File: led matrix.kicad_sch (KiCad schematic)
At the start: 88 parts, among them SW49 Slide_DPDT_SS22D06

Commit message: parpar v2 RC2
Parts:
- added JP3: Switch bypass, Jumper:SolderJumper-2_P1.3mm_Open_TrianglePad1.0x1.5mm, symbol Jumper:SolderJumper_2_Open
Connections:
- net +5V: now also JP3.1 (A)
- net PRI_LO: now also JP3.2 (B)
- net led_data: now also R1.2; no longer R1.1
- net at D3.3 (DIN): now also R1.1; no longer R1.2
- net led_out: now reaches D44.2 (DOUT)
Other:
- moved on the sheet: JP1

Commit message: parpar v2 RC3
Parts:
- R1: symbol Device:R -> Device:R_US
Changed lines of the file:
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@@
 	)
 	(symbol
-		(lib_id "Device:R")
+		(lib_id "Device:R_US")
 		(at 16.51 33.02 0)
 		(mirror x)
@@
 		(on_board yes)
 		(dnp no)
-		(fields_autoplaced yes)
 		(property "Reference" "R1"
-			(at 19.05 34.2901 0)
+			(at 19.304 33.782 90)
 			(effects
 				(font
 					(size 1.27 1.27)
 				)
-				(justify left)
+				(justify right)
 			)
 		)
 		(property "Value" "R470"
-			(at 19.05 31.7501 0)
+			(at 21.59 34.798 90)
 			(effects
 				(font
 					(size 1.27 1.27)
 				)
-				(justify left)
+				(justify right)
 			)
 		)
 		(property "Footprint" "Resistor_SMD:R_0805_2012Metric"
-			(at 14.732 33.02 90)
+			(at 17.526 32.766 90)
 			(effects
 				(font
@@
 			)
 		)
-		(property "Description" "Resistor"
+		(property "Description" "Resistor, US symbol"
 			(at 16.51 33.02 0)
 			(effects

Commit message: parpar v2 RC4
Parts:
- removed JP3: Switch bypass, Jumper:SolderJumper-2_P1.3mm_Open_TrianglePad1.0x1.5mm, symbol Jumper:SolderJumper_2_Open
- removed SW49: Slide_DPDT_SS22D06, Button_Switch_SMD:SW_DPDT_CK_JS202011JCQN, symbol PCM_4ms_Switch:Slide_DPDT_SS22D06
- added C48: 0.1uF, Capacitor_SMD:C_0805_2012Metric, symbol Device:C
- added R6: R500, Resistor_SMD:R_0805_2012Metric, symbol Device:R_US
- added R7: 10k, Resistor_SMD:R_0805_2012Metric, symbol Device:R_US
- added U13: SN74LV1T125DCK, Package_TO_SOT_SMD:SOT-353_SC-70-5, symbol Logic_LevelTranslator:SN74LV1T125DCK
- R1: value R470 -> R500
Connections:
- net PRI_LO is gone; now on net +5V: C1.1, C10.1, C11.1, C12.1, C13.1, C14.1, C15.1, C16.1, C17.1, C18.1, C19.1, C2.1, C20.1, C21.1, C22.1, C23.1, C24.1, C25.1, C26.1, C27.1, C28.1, C29.1, C3.1, C30.1, C31.1, C32.1, C33.1, C34.1, C35.1, C36.1, C37.1, C38.1, C39.1, C4.1, C40.1, C41.1, C42.1, C43.1, C5.1, C6.1, C7.1, C8.1, C9.1, D10.1 (VDD), D11.1 (VDD), D12.1 (VDD), D13.1 (VDD), D14.1 (VDD), D15.1 (VDD), D16.1 (VDD), D17.1 (VDD), D18.1 (VDD), D19.1 (VDD), D20.1 (VDD), D21.1 (VDD), D22.1 (VDD), D23.1 (VDD), D24.1 (VDD), D25.1 (VDD), D26.1 (VDD), D27.1 (VDD), D28.1 (VDD), D29.1 (VDD), D3.1 (VDD), D30.1 (VDD), D31.1 (VDD), D32.1 (VDD), D33.1 (VDD), D34.1 (VDD), D35.1 (VDD), D36.1 (VDD), D37.1 (VDD), D38.1 (VDD), D39.1 (VDD), D4.1 (VDD), D40.1 (VDD), D41.1 (VDD), D42.1 (VDD), D43.1 (VDD), D44.1 (VDD), D5.1 (VDD), D6.1 (VDD), D7.1 (VDD), D8.1 (VDD), D9.1 (VDD)
- net +5V: now also C48.1
- net GND: now also R7.1, U13.3 (GND)
- net led_data: now also U13.4 (Y); no longer JP1.2 (C)
- net led_out: now also R6.2; no longer D44.2 (DOUT)
- new net: R7.2, U13.1 (~{OE})
- new net: C48.2, U13.5 (VCC)
- new net: D44.2 (DOUT), R6.1
- new net led_data_in: JP1.2 (C), U13.2 (A)
- no-connect marks 1 -> 0
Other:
- note added: "led data"
- note added: "led power input"
- note removed: "led data selector"
- note removed: "led power switch"
- moved on the sheet: C1, C10, C11, C12, C13, C14, C15, C16, C17, C18, C19, C2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

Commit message: parpar v2 RC6
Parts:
- JP1: value SolderJumper_3_Bridged12 -> data select
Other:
- note added: "rgb data"
- note added: "rgb power in"
- note removed: "led data"
- note removed: "led power input"
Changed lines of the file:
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@@
 	)
 	(rectangle
-		(start 172.72 78.74)
+		(start 173.355 72.39)
 		(end 284.48 160.02)
 		(stroke
@@
 		)
 	)
-	(text "led data"
+	(text "rgb data"
 		(exclude_from_sim no)
-		(at 218.948 16.51 0)
+		(at 214.884 16.764 0)
 		(effects
 			(font
@@
 		)
 	)
-	(text "led power input"
+	(text "rgb power in"
 		(exclude_from_sim no)
-		(at 181.61 16.51 0)
+		(at 179.832 16.764 0)
 		(effects
 			(font
@@
 			)
 		)
-		(property "Value" "SolderJumper_3_Bridged12"
+		(property "Value" "data select"
 			(at 228.6 24.13 0)
 			(effects

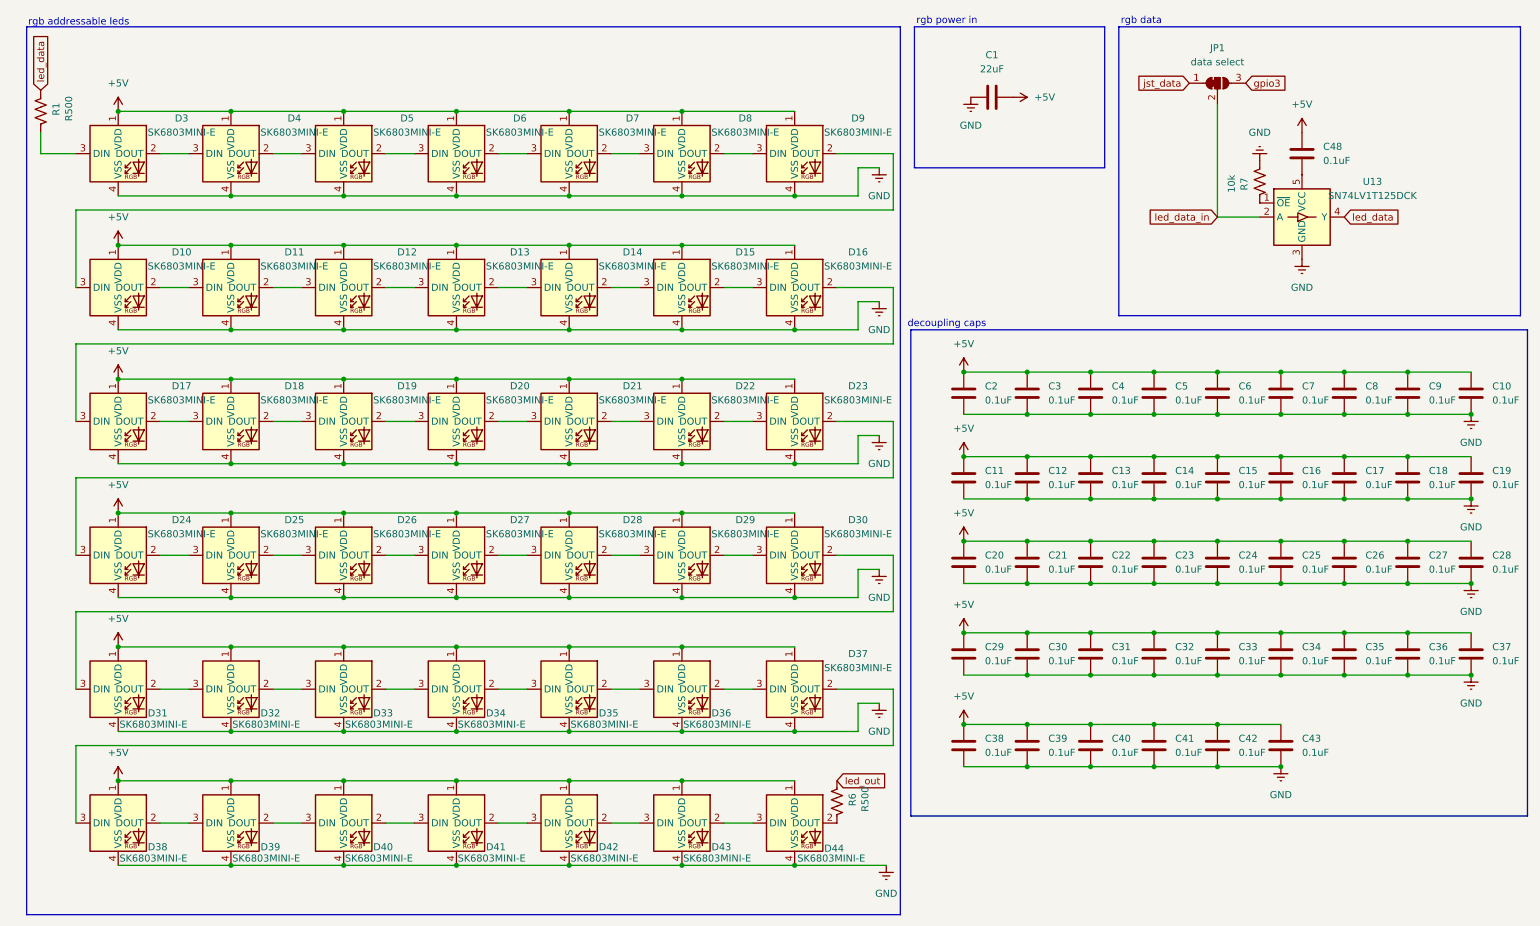
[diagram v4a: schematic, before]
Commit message: another resistor value to a real-world existing part
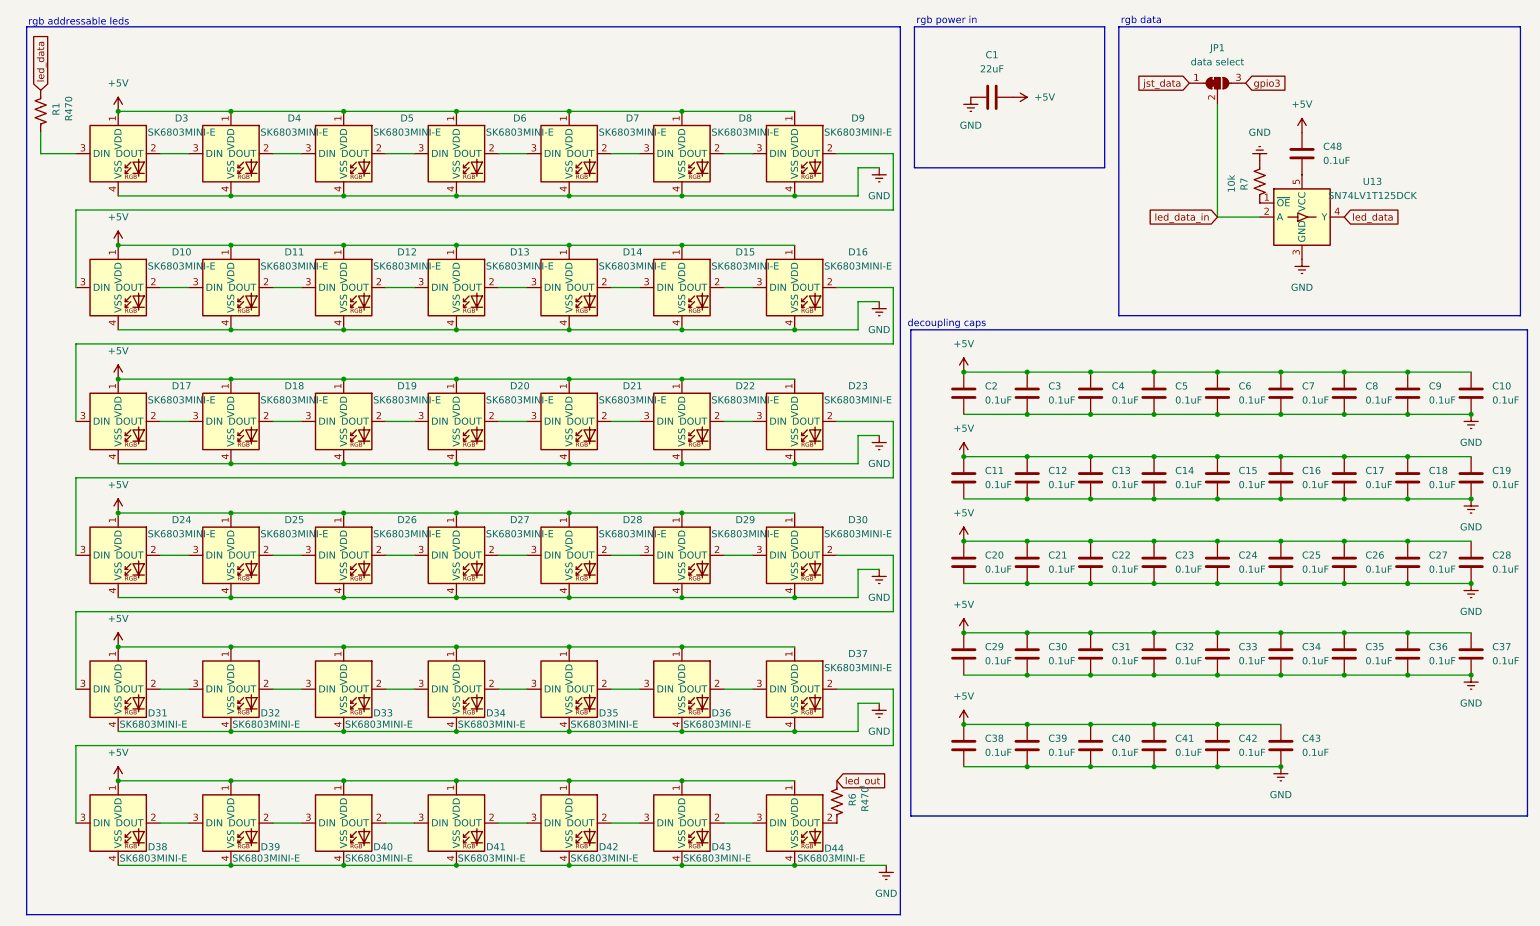
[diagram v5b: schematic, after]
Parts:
- R1, R6: value R500 -> R470
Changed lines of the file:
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@@
 			)
 		)
-		(property "Value" "R500"
+		(property "Value" "R470"
 			(at 21.59 34.798 90)
 			(effects
@@
 			)
 		)
-		(property "Value" "R500"
+		(property "Value" "R470"
 			(at 165.1 159.258 90)
 			(effects

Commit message: column resistors to further bolster protection against esd events and shorts
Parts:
- C10, C11, C12, C13, C14, C15, C16, C17, C18, C19, C2, C20, C21, C22, C23, C24, C25, C26, C27, C28, C29, C3, C30, C31, C32, C33, C34, C35, C36, C37, C38, C39, C4, C40, C41, C42, C43, C48, C5, C6, C7, C8, C9: footprint Capacitor_SMD:C_0805_2012Metric -> Capacitor_SMD:C_0603_1608Metric
- R7: footprint Resistor_SMD:R_0805_2012Metric -> Resistor_SMD:R_0603_1608Metric
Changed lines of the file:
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@@
 	(title_block
 		(title "coquette parpar led matrix")
-		(date "2025-01-19")
+		(date "2025-01-20")
 		(rev "2.0")
 	)
@@
 			)
 		)
-		(property "Footprint" "Capacitor_SMD:C_0805_2012Metric"
+		(property "Footprint" "Capacitor_SMD:C_0603_1608Metric"
 			(at 239.0648 102.87 0)
 			(effects
@@
 			)
 		)
-		(property "Footprint" "Capacitor_SMD:C_0805_2012Metric"
+		(property "Footprint" "Capacitor_SMD:C_0603_1608Metric"
 			(at 206.7052 134.62 0)
 			(effects
@@
 			)
 		)
-		(property "Footprint" "Capacitor_SMD:C_0805_2012Metric"
+		(property "Footprint" "Capacitor_SMD:C_0603_1608Metric"
 			(at 229.5652 151.13 0)
 			(effects
@@
 			)
 		)
-		(property "Footprint" "Capacitor_SMD:C_0805_2012Metric"
+		(property "Footprint" "Capacitor_SMD:C_0603_1608Metric"
 			(at 216.2048 87.63 0)
 			(effects
@@
 			)
 		)
-		(property "Footprint" "Capacitor_SMD:C_0805_2012Metric"
+		(property "Footprint" "Capacitor_SMD:C_0603_1608Metric"
 			(at 181.9148 102.87 0)
 			(effects
@@
 			)
 		)
-		(property "Footprint" "Capacitor_SMD:C_0805_2012Metric"
+		(property "Footprint" "Capacitor_SMD:C_0603_1608Metric"
 			(at 181.9148 87.63 0)
 			(effects
@@
 			)
 		)
-		(property "Footprint" "Capacitor_SMD:C_0805_2012Metric"
+		(property "Footprint" "Capacitor_SMD:C_0603_1608Metric"
 			(at 227.6348 87.63 0)
 			(effects
@@
 			)
 		)
-		(property "Footprint" "Capacitor_SMD:C_0805_2012Metric"
+		(property "Footprint" "Capacitor_SMD:C_0603_1608Metric"
 			(at 240.9952 134.62 0)
 			(effects
@@
 			)
 		)
-		(property "Footprint" "Capacitor_SMD:C_0805_2012Metric"
+		(property "Footprint" "Capacitor_SMD:C_0603_1608Metric"
 			(at 252.4252 118.11 0)
 			(effects
@@
 			)
 		)
-		(property "Footprint" "Capacitor_SMD:C_0805_2012Metric"
+		(property "Footprint" "Capacitor_SMD:C_0603_1608Metric"
 			(at 252.4252 134.62 0)
 			(effects
@@
 			)
 		)
-		(property "Footprint" "Capacitor_SMD:C_0805_2012Metric"
+		(property "Footprint" "Capacitor_SMD:C_0603_1608Metric"
 			(at 206.7052 118.11 0)
 			(effects
@@
 			)
 		)
-		(property "Footprint" "Capacitor_SMD:C_0805_2012Metric"
+		(property "Footprint" "Capacitor_SMD:C_0603_1608Metric"
 			(at 239.0648 87.63 0)
 			(effects
@@
 			)
 		)
-		(property "Footprint" "Resistor_SMD:R_0805_2012Metric"
+		(property "Footprint" "Resistor_SMD:R_0603_1608Metric"
 			(at 235.204 45.974 90)
 			(effects
@@
 			)
 		)
-		(property "Footprint" "Capacitor_SMD:C_0805_2012Metric"
+		(property "Footprint" "Capacitor_SMD:C_0603_1608Metric"
 			(at 263.8552 118.11 0)
 			(effects
@@
 			)
 		)
-		(property "Footprint" "Capacitor_SMD:C_0805_2012Metric"
+		(property "Footprint" "Capacitor_SMD:C_0603_1608Metric"
 			(at 275.2852 118.11 0)
 			(effects
@@
 			)
 		)
-		(property "Footprint" "Capacitor_SMD:C_0805_2012Metric"
+		(property "Footprint" "Capacitor_SMD:C_0603_1608Metric"
 			(at 193.3448 87.63 0)
 			(effects
@@
 			)
 		)
-		(property "Footprint" "Capacitor_SMD:C_0805_2012Metric"
+		(property "Footprint" "Capacitor_SMD:C_0603_1608Metric"
 			(at 261.9248 102.87 0)
 			(effects
@@
 			)
 		)
-		(property "Footprint" "Capacitor_SMD:C_0805_2012Metric"
+		(property "Footprint" "Capacitor_SMD:C_0603_1608Metric"
 			(at 206.7052 151.13 0)
 			(effects
@@
 			)
 		)
-		(property "Footprint" "Capacitor_SMD:C_0805_2012Metric"
+		(property "Footprint" "Capacitor_SMD:C_0603_1608Metric"
 			(at 263.8552 134.62 0)
 			(effects
@@
 			)
 		)
-		(property "Footprint" "Capacitor_SMD:C_0805_2012Metric"
+		(property "Footprint" "Capacitor_SMD:C_0603_1608Metric"
 			(at 204.7748 102.87 0)
 			(effects
@@
 			)
 		)
-		(property "Footprint" "Capacitor_SMD:C_0805_2012Metric"
+		(property "Footprint" "Capacitor_SMD:C_0603_1608Metric"
 			(at 250.4948 87.63 0)
 			(effects
@@
 			)
 		)
-		(property "Footprint" "Capacitor_SMD:C_0805_2012Metric"
+		(property "Footprint" "Capacitor_SMD:C_0603_1608Metric"
 			(at 229.5652 118.11 0)
 			(effects
@@
 			)
 		)
-		(property "Footprint" "Capacitor_SMD:C_0805_2012Metric"
+		(property "Footprint" "Capacitor_SMD:C_0603_1608Metric"
 			(at 250.4948 102.87 0)
 			(effects
@@
 			)
 		)
-		(property "Footprint" "Capacitor_SMD:C_0805_2012Metric"
+		(property "Footprint" "Capacitor_SMD:C_0603_1608Metric"
 			(at 218.1352 151.13 0)
 			(effects
@@
 			)
 		)
-		(property "Footprint" "Capacitor_SMD:C_0805_2012Metric"
+		(property "Footprint" "Capacitor_SMD:C_0603_1608Metric"
 			(at 183.8452 134.62 0)
 			(effects
@@
 			)
 		)
-		(property "Footprint" "Capacitor_SMD:C_0805_2012Metric"
+		(property "Footprint" "Capacitor_SMD:C_0603_1608Metric"
 			(at 195.2752 118.11 0)
 			(effects
@@
 			)
 		)
-		(property "Footprint" "Capacitor_SMD:C_0805_2012Metric"
+		(property "Footprint" "Capacitor_SMD:C_0603_1608Metric"
 			(at 275.2852 134.62 0)
 			(effects
@@
 			)
 		)
-		(property "Footprint" "Capacitor_SMD:C_0805_2012Metric"
+		(property "Footprint" "Capacitor_SMD:C_0603_1608Metric"
 			(at 195.2752 151.13 0)
 			(effects
@@
 			)
 		)
-		(property "Footprint" "Capacitor_SMD:C_0805_2012Metric"
+		(property "Footprint" "Capacitor_SMD:C_0603_1608Metric"
 			(at 242.8748 44.45 0)
 			(effects
@@
 			)
 		)
-		(property "Footprint" "Capacitor_SMD:C_0805_2012Metric"
+		(property "Footprint" "Capacitor_SMD:C_0603_1608Metric"
 			(at 218.1352 134.62 0)
 			(effects
@@
 			)
 		)
-		(property "Footprint" "Capacitor_SMD:C_0805_2012Metric"
+		(property "Footprint" "Capacitor_SMD:C_0603_1608Metric"
 			(at 275.2852 102.87 0)
 			(effects
@@
 			)
 		)
-		(property "Footprint" "Capacitor_SMD:C_0805_2012Metric"
+		(property "Footprint" "Capacitor_SMD:C_0603_1608Metric"
 			(at 227.6348 102.87 0)
 			(effects
@@
 			)
 		)
-		(property "Footprint" "Capacitor_SMD:C_0805_2012Metric"
+		(property "Footprint" "Capacitor_SMD:C_0603_1608Metric"
 			(at 240.9952 118.11 0)
 			(effects
@@
 			)
 		)
-		(property "Footprint" "Capacitor_SMD:C_0805_2012Metric"
+		(property "Footprint" "Capacitor_SMD:C_0603_1608Metric"
 			(at 218.1352 118.11 0)
 			(effects
@@
 			)
 		)
-		(property "Footprint" "Capacitor_SMD:C_0805_2012Metric"
+		(property "Footprint" "Capacitor_SMD:C_0603_1608Metric"
 			(at 183.8452 118.11 0)
 			(effects
@@
 			)
 		)
-		(property "Footprint" "Capacitor_SMD:C_0805_2012Metric"
+		(property "Footprint" "Capacitor_SMD:C_0603_1608Metric"
 			(at 240.9952 151.13 0)
 			(effects
@@
 			)
 		)
-		(property "Footprint" "Capacitor_SMD:C_0805_2012Metric"
+		(property "Footprint" "Capacitor_SMD:C_0603_1608Metric"
 			(at 204.7748 87.63 0)
 			(effects
@@
 			)
 		)
-		(property "Footprint" "Capacitor_SMD:C_0805_2012Metric"
+		(property "Footprint" "Capacitor_SMD:C_0603_1608Metric"
 			(at 216.2048 102.87 0)
 			(effects
@@
 			)
 		)
-		(property "Footprint" "Capacitor_SMD:C_0805_2012Metric"
+		(property "Footprint" "Capacitor_SMD:C_0603_1608Metric"
 			(at 261.9248 87.63 0)
 			(effects
@@
 			)
 		)
-		(property "Footprint" "Capacitor_SMD:C_0805_2012Metric"
+		(property "Footprint" "Capacitor_SMD:C_0603_1608Metric"
 			(at 193.3448 102.87 0)
 			(effects
@@
 			)
 		)
-		(property "Footprint" "Capacitor_SMD:C_0805_2012Metric"
+		(property "Footprint" "Capacitor_SMD:C_0603_1608Metric"
 			(at 229.5652 134.62 0)
 			(effects
@@
 			)
 		)
-		(property "Footprint" "Capacitor_SMD:C_0805_2012Metric"
+		(property "Footprint" "Capacitor_SMD:C_0603_1608Metric"
 			(at 183.8452 151.13 0)
 			(effects
@@
 			)
 		)
-		(property "Footprint" "Capacitor_SMD:C_0805_2012Metric"
+		(property "Footprint" "Capacitor_SMD:C_0603_1608Metric"
 			(at 273.3548 87.63 0)
 			(effects
@@
 			)
 		)
-		(property "Footprint" "Capacitor_SMD:C_0805_2012Metric"
+		(property "Footprint" "Capacitor_SMD:C_0603_1608Metric"
 			(at 195.2752 134.62 0)
 			(effects

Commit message: v2 final ready to order
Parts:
- removed C10, C11, C12, C13, C14, C15, C16, C17, C18, C19, C2, C20, C21, C22, C23, C24, C25, C26, C27, C28, C29, C3, C30, C31, C32, C33, C34, C35, C36, C37, C38, C39, C4, C41, C42, C43, C48, C5, C6, C7, C8, C9: 0.1uF, Capacitor_SMD:C_0603_1608Metric, symbol Device:C
- removed D10, D11, D12, D13, D14, D15, D16, D17, D18, D19, D20, D21, D22, D23, D24, D25, D26, D27, D28, D29, D3, D30, D31, D32, D33, D34, D35, D36, D37, D38, D39, D4, D40, D41, D42, D43, D44, D5, D6, D7, D8, D9: SK6803MINI-E, marbastlib-various:LED_6028R, symbol marbastlib-various:SK6812MINI-E
- removed JP1: data select, Jumper:SolderJumper-3_P1.3mm_Bridged12_RoundedPad1.0x1.5mm, symbol Jumper:SolderJumper_3_Bridged12
- removed R1, R6: R470, Resistor_SMD:R_0805_2012Metric, symbol Device:R_US
- removed R7: 10k, Resistor_SMD:R_0603_1608Metric, symbol Device:R_US
- removed U13: SN74LV1T125DCK, Package_TO_SOT_SMD:SOT-353_SC-70-5, symbol Logic_LevelTranslator:SN74LV1T125DCK
- added C55: 1uF, Capacitor_SMD:C_0603_1608Metric, symbol Device:C
- added D36, D37, D38, D39: LED, PCM_LED_SMD_AKL:LED_PLCC_2835, symbol Device:LED
- added J41, J42: Conn_01x03_MountingPin, Connector_JST:JST_SH_SM03B-SRSS-TB_1x03-1MP_P1.00mm_Horizontal, symbol Connector_Generic_MountingPin:Conn_01x03_MountingPin
- added U40: LP5814DRLR, Package_TO_SOT_SMD:SOT-583-8, symbol gachlilit:LP5814DRLR
- C40: value 0.1uF -> 10uF; footprint Capacitor_SMD:C_0603_1608Metric -> Capacitor_SMD:C_0805_2012Metric
- C5: renamed from C1; value 22uF -> 10uF
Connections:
- net GND: now also C55.2, J41.3 (Pin_3), J41.MP (MountPin), J42.3 (Pin_3), J42.MP (MountPin), U40.3 (GND)
- net +5V renamed VCC
- net VCC: now also C55.1, D36.2 (A), D37.2 (A), D38.2 (A), D39.2 (A), U40.4 (VCC); no longer C5.1
- new net VDC: C5.1, J41.2 (Pin_2), J42.2 (Pin_2)
- new net argb_conn: J41.1 (Pin_1), J42.1 (Pin_1)
- new net scl: U40.1 (SCL)
- new net sda: U40.2 (SDA)
- new net uv1: D37.1 (K), U40.8 (OUT0)
- new net uv2: D36.1 (K), U40.7 (OUT1)
- new net uv3: D38.1 (K), U40.6 (OUT2)
- new net uv4: D39.1 (K), U40.5 (OUT3)
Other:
- note added: "argb in"
- note added: "argb out"
- note added: "blacklight"
- note removed: "decoupling caps"
- note removed: "rgb addressable leds"
- note removed: "rgb data"
- moved on the sheet: C5
